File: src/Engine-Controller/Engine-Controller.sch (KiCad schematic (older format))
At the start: 22 parts, among them J1 Jumper_NO, J2 Jumper_NO, U1 STM32H750VBTx

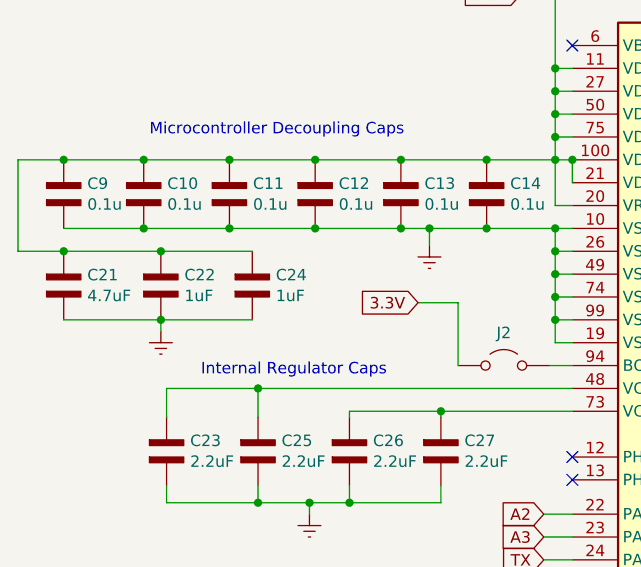
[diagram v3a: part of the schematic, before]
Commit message: finished routing rev3.0
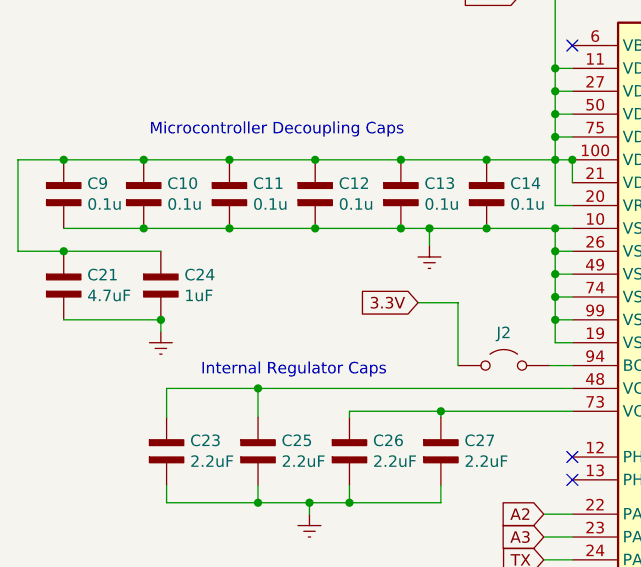
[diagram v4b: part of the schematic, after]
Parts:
- removed C22: 1uF, Engine-Controller:CAP_0603, symbol Engine-Controller:CAP_0603
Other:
- moved on the sheet: C24
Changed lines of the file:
@@
 Text Notes 1375 2800 0    50   ~ 0
 Internal Regulator Caps
+Connection ~ 775  2250
 $Comp
-L Engine-Controller:CAP_0603 C22
-U 1 1 61A50FA8
+L Engine-Controller:CAP_0603 C24
+U 1 1 61A571EB
 P 1200 2400
-F 0 "C22" V 1154 2503 50  0000 L CNN
+F 0 "C24" V 1154 2503 50  0000 L CNN
 F 1 "1uF" V 1245 2503 50  0000 L CNN
 F 2 "Engine-Controller:CAP_0603" H 1100 2000 50  0001 L BNN
@@
 $EndComp
 Wire Wire Line
-	775  2250 1200 2250
-Connection ~ 775  2250
-$Comp
-L Engine-Controller:CAP_0603 C24
-U 1 1 61A571EB
-P 1600 2400
-F 0 "C24" V 1554 2503 50  0000 L CNN
-F 1 "1uF" V 1645 2503 50  0000 L CNN
-F 2 "Engine-Controller:CAP_0603" H 1500 2000 50  0001 L BNN
-F 3 "" H 1550 2400 50  0001 L BNN
-	1    1600 2400
-	0    1    1    0
-$EndComp
-Wire Wire Line
-	1200 2250 1600 2250
-Connection ~ 1200 2250
-Wire Wire Line
 	1200 2550 775  2550
-Wire Wire Line
-	1200 2550 1600 2550
 Connection ~ 1200 2550
 Wire Wire Line
@@
 Wire Wire Line
 	2500 2475 2325 2475
+Wire Wire Line
+	775  2250 1200 2250
 $EndSCHEMATC
